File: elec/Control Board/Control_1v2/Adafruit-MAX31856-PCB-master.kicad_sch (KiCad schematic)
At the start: 8 parts, among them J10 MCP9600, J8 MCP9600, J9 MCP9600

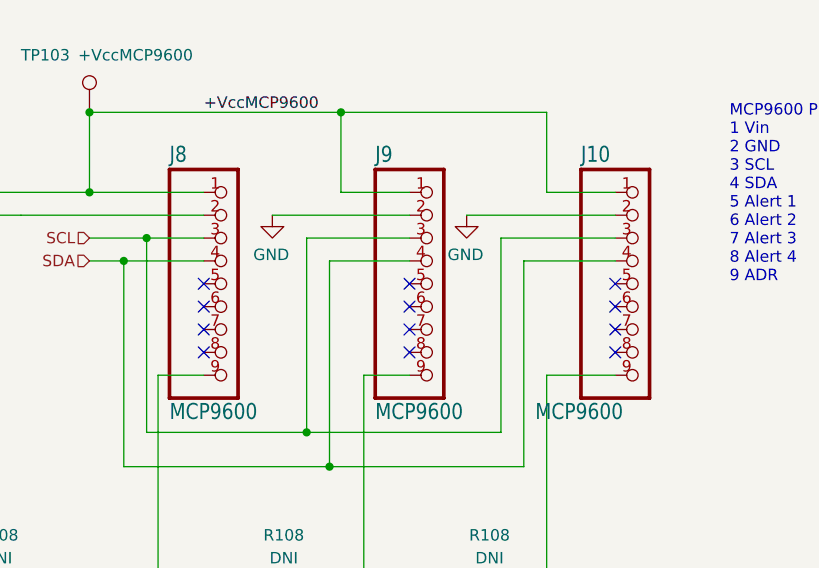
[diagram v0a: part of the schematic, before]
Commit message: PCB V1.2. Add 3d model for power supply footprint. Set many headers connectors for DNI on schematic and PCB.
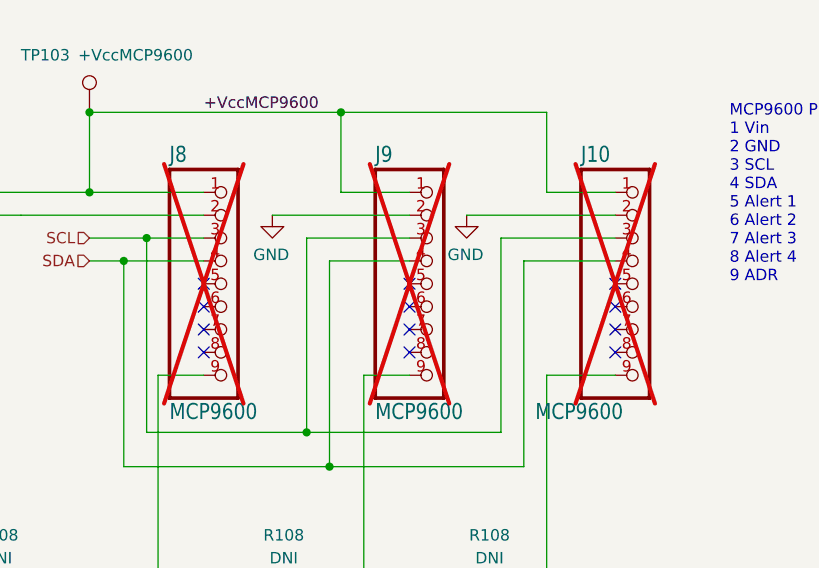
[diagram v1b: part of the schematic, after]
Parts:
- J10, J8, J9: now not fitted; now left out of the parts list
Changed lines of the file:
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@@
   )
   (symbol (lib_id "Control v1-eagle-import:HEADER-1X970MIL") (at 161.29 77.47 0) (unit 1)
-    (in_bom yes) (on_board yes) (dnp no)
+    (in_bom no) (on_board yes) (dnp yes)
     (property "Reference" "J10" (at 154.94 64.135 0)
       (effects (font (size 1.778 1.5113)) (justify left bottom))
@@
   )
   (symbol (lib_id "Control v1-eagle-import:HEADER-1X970MIL") (at 138.43 77.47 0) (unit 1)
-    (in_bom yes) (on_board yes) (dnp no)
+    (in_bom no) (on_board yes) (dnp yes)
     (property "Reference" "J9" (at 132.08 64.135 0)
       (effects (font (size 1.778 1.5113)) (justify left bottom))
@@
   )
   (symbol (lib_id "Control v1-eagle-import:HEADER-1X970MIL") (at 115.57 77.47 0) (unit 1)
-    (in_bom yes) (on_board yes) (dnp no)
+    (in_bom no) (on_board yes) (dnp yes)
     (property "Reference" "J8" (at 109.22 64.135 0)
       (effects (font (size 1.778 1.5113)) (justify left bottom))

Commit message: PCB V1.2. Add test points of many colors.
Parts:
- TP103: Cost NA -> 0.0696; Distributor 1 (none) -> JLCPCB; Distributor 1 PN (none) -> C5277086; MPN (none) -> RH-5000; Manufacturer (none) -> ronghe
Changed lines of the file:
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@@
       (effects (font (size 1.27 1.27)) hide)
     )
-    (property "Cost" "NA" (at 100.33 58.42 0)
+    (property "Cost" "0.0696" (at 100.33 58.42 0)
       (effects (font (size 1.27 1.27)) hide)
     )
+    (property "Description" "Test Points/Test Rings ROHS red" (at 100.33 58.42 0)
+      (effects (font (size 1.27 1.27)) hide)
+    )
+    (property "Distributor 1 PN" "C5277086" (at 100.33 58.42 0)
+      (effects (font (size 1.27 1.27)) hide)
+    )
+    (property "Distributor 1" "JLCPCB" (at 100.33 58.42 0)
+      (effects (font (size 1.27 1.27)) hide)
+    )
+    (property "MPN" "RH-5000 " (at 100.33 58.42 0)
+      (effects (font (size 1.27 1.27)) hide)
+    )
+    (property "Manufacturer" "ronghe " (at 100.33 58.42 0)
+      (effects (font (size 1.27 1.27)) hide)
+    )
